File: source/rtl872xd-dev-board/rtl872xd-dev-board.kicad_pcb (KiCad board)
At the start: 4 copper layers, 26 x 39.2 mm, 59 parts, among them J1 Conn_Coaxial, J2 Bus_M.2_Socket_B, U1 RTL8722DM, U2 W25Q128JVS, U3 W25Q16JV, U4 LM809, Y1 40MHz

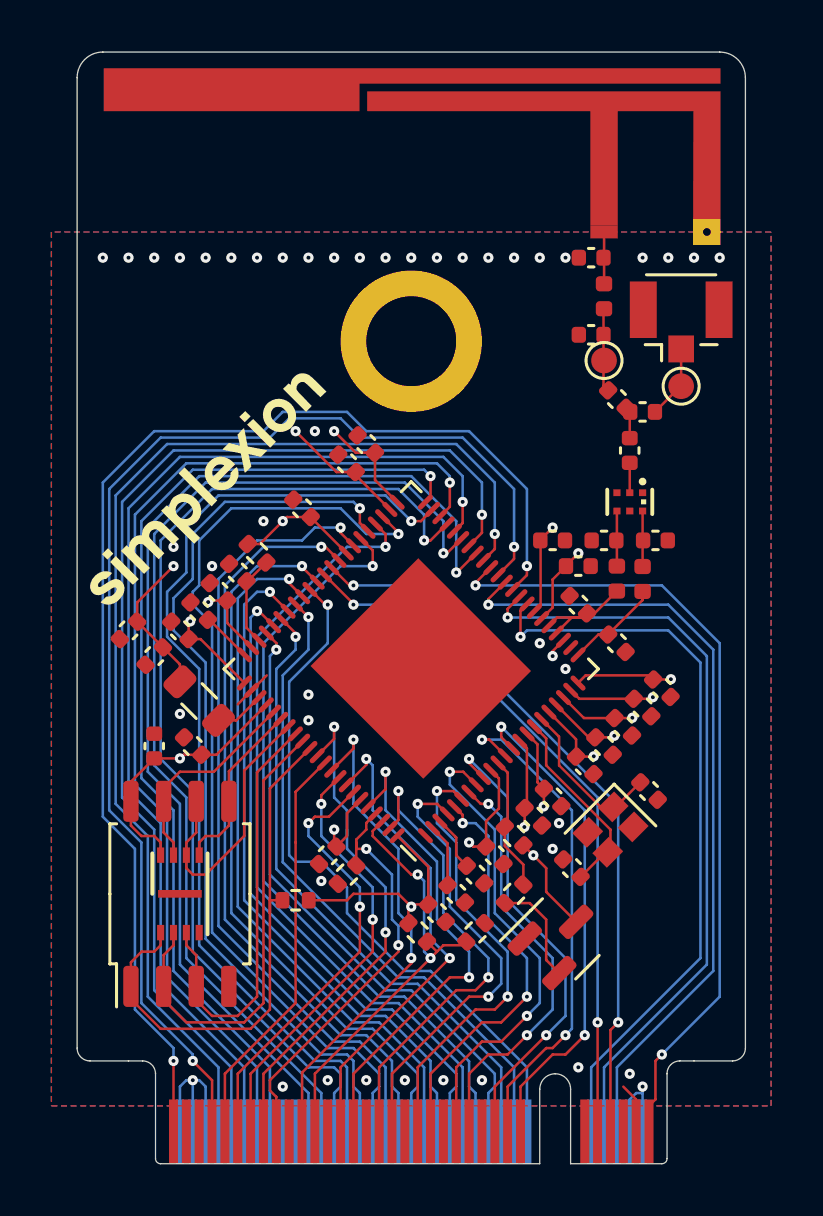
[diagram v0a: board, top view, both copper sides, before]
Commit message: added TC2030 debug ports
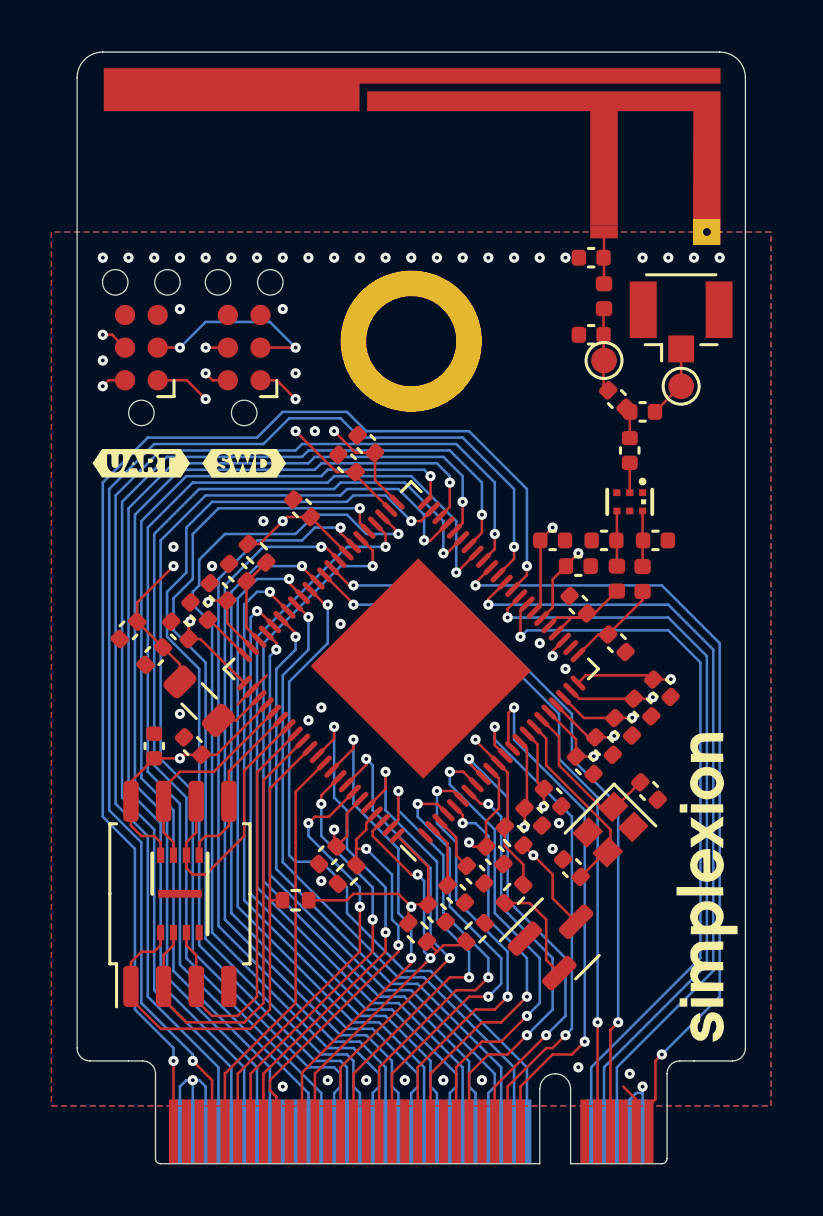
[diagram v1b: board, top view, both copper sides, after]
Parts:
- added J3: Conn_ARM_SWD_TagConnect_TC2030-NL, Connector:Tag-Connect_TC2030-IDC-NL_2x03_P1.27mm_Vertical, F.Cu at (120.5, 113.5)
- added J4: Conn_ARM_SWD_TagConnect_TC2030-NL, Connector:Tag-Connect_TC2030-IDC-NL_2x03_P1.27mm_Vertical, F.Cu at (116.5, 113.5)
- added kibuzzard-6492E3AE: G***, kibuzzard-6492E3AE, F.Cu at (120.5, 118.0)
- added kibuzzard-6492E3B2: G***, kibuzzard-6492E3B2, F.Cu at (116.5, 118.0)
- moved G*** 24.9 mm to (138.5, 134.5), turned to 90 degrees
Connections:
- net /PA27 renamed /SWD.SWDIO
- net /PA7 renamed /UART_{LOG}.TX
- net /PA8 renamed /UART_{LOG}.RX
- net /Power & Clock/CHIP_EN renamed /~{RESET}
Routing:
- net /~{RESET}: track 5.23 -> 42.4 mm, vias 0 -> 3
- net /UART_{LOG}.RX: track 19.5 -> 48.2 mm, vias 2 -> 3
- net /UART_{LOG}.TX: track 19.5 -> 44.5 mm, vias 2 -> 3
- net /SWD.SWDIO: track 30.7 -> 43.3 mm, vias 1 -> 2
- net /PB3: track 27.6 -> 39.4 mm, vias 1 -> 2
- net +3V3: track 154.0 -> 164.6 mm, vias 14 -> 16
- net VDD: track 76.4 -> 78.6 mm
- net /USB.D-: track 27.2 -> 28.3 mm
- net /USB.D+: track 27.8 -> 28.8 mm
- net /PA24: track 36.4 -> 35.8 mm
- net GND: vias 44 -> 49

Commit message: resolve all ERC error, reduce number of warnings
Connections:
- net +3V3 renamed +3.3V

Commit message: tidied up like Marie Kondo
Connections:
- net /PB3 renamed /SWD.SWCLK
- net /USB.D+ renamed /PA26
- net /USB.D- renamed /PA25

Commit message: first production version
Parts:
- added TP3: TestPoint, TestPoint:TestPoint_Pad_D1.0mm, F.Cu at (136.5, 138.0)
- added TP4: TestPoint, TestPoint:TestPoint_Pad_D1.0mm, F.Cu at (134.5, 138.0)
- added TP5: TestPoint, TestPoint:TestPoint_Pad_D1.0mm, F.Cu at (115.5, 118.0)
- added TP6: TestPoint, TestPoint:TestPoint_Pad_D1.0mm, F.Cu at (115.5, 120.0)
- added TP7: TestPoint, TestPoint:TestPoint_Pad_D1.0mm, F.Cu at (117.5, 120.0)
- added TP8: TestPoint, TestPoint:TestPoint_Pad_D1.0mm, F.Cu at (117.5, 118.0)
- added TP9: TestPoint, TestPoint:TestPoint_Pad_D1.0mm, F.Cu at (136.5, 136.0)
- moved kibuzzard-6492E3AE 8.50 mm to (120.5, 109.5)
- moved kibuzzard-6492E3B2 8.50 mm to (116.5, 109.5)
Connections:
- net /PA25 renamed D-
- net /PA26 renamed D+
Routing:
- net +3.3V: track 164.6 -> 168.2 mm
- net VDD: track 78.6 -> 81.9 mm
- net /~{RESET}: track 42.4 -> 45.2 mm, vias 3 -> 4
- net D+: track 28.8 -> 30.8 mm
- net D-: track 28.3 -> 29.8 mm
- net GND: vias 49 -> 55
